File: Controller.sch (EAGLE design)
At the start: 45 parts, among them SW1 MULTICOLOR_BUTTON, SW2 MULTICOLOR_BUTTON, SW3 MULTICOLOR_BUTTON, SW4 MULTICOLOR_BUTTON, SW5 MULTICOLOR_BUTTON, SW6 MULTICOLOR_BUTTON, SW7 MULTICOLOR_BUTTON, SW8 MULTICOLOR_BUTTON, U1 ATMEGA328-PU, U2 DRV5053VAQLPGM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

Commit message: Added switch and LED
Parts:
- added R7: 1k, rcl:R-US_R1206
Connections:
- new net N$2: R7.2, U1.PCINT14/!RESET/PC6
- net +5V: now also R7.1
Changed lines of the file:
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@@
 <part name="C11" library="rcl" library_urn="urn:adsk.eagle:library:334" deviceset="C-US" device="C1206" package3d_urn="urn:adsk.eagle:package:23618/2" value="0.1u"/>
 <part name="GND4" library="supply1" library_urn="urn:adsk.eagle:library:371" deviceset="GND" device=""/>
+<part name="R7" library="rcl" library_urn="urn:adsk.eagle:library:334" deviceset="R-US_" device="R1206" package3d_urn="urn:adsk.eagle:package:23540/2" value="1k"/>
+<part name="P+11" library="supply1" library_urn="urn:adsk.eagle:library:371" deviceset="+5V" device=""/>
 </parts>
 <sheets>
@@
 <attribute name="VALUE" x="203.2" y="127" size="1.778" layer="96" rot="R90"/>
 </instance>
+<instance part="R7" gate="G$1" x="86.36" y="147.32" smashed="yes" rot="R270">
+<attribute name="NAME" x="80.2386" y="148.59" size="1.778" layer="95" rot="R270"/>
+<attribute name="VALUE" x="83.058" y="148.59" size="1.778" layer="96" rot="R270"/>
+</instance>
+<instance part="P+11" gate="1" x="86.36" y="157.48" smashed="yes">
+<attribute name="VALUE" x="83.82" y="152.4" size="1.778" layer="96" rot="R90"/>
+</instance>
 </instances>
 <busses>
@@
 <wire x1="175.26" y1="119.38" x2="175.26" y2="121.92" width="0.1524" layer="91"/>
 <junction x="175.26" y="121.92"/>
+</segment>
+<segment>
+<pinref part="P+11" gate="1" pin="+5V"/>
+<pinref part="R7" gate="G$1" pin="1"/>
+<wire x1="86.36" y1="154.94" x2="86.36" y2="152.4" width="0.1524" layer="91"/>
 </segment>
 </net>
@@
 </segment>
 </net>
+<net name="N$2" class="0">
+<segment>
+<pinref part="R7" gate="G$1" pin="2"/>
+<wire x1="86.36" y1="142.24" x2="86.36" y2="139.7" width="0.1524" layer="91"/>
+<pinref part="U1" gate="A" pin="PCINT14/!RESET/PC6"/>
+<wire x1="86.36" y1="139.7" x2="96.52" y2="139.7" width="0.1524" layer="91"/>
+</segment>
+</net>

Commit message: finished?
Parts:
- added J1: 282834-4, 282834-4:282834-4
- added J2: 282834-2, 282834-2:282834-2
- added J3: 825457-3, 825457-3:825457-3
- added R10: 150, rcl:R-US_R1206
- added R11: 475k, rcl:R-US_R1206
- added R12: 100k, rcl:R-US_R1206
- added R8, R9: 1k, rcl:R-US_R1206
- added SW9: 3PDT, Controller:3PDT
- added U$2: LED, Controller:LED
- added U$3: BSS138L, BSS138L:BSS138L
- added U6: (no value), Controller:SSM6P40TULFCT-ND
- C5: value 10U -> 10u
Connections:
- removed net N$2: R7.2, U1.PCINT14/!RESET/PC6
- removed net VBAT: C12.1, C13.1, U5.VIN
- new net CLK: J3.3, U1.PB5/SCK/PCINT5
- new net MISO: J3.1, R9.2, U1.PB4/MISO/PCINT4
- new net MOSI: J3.4, R8.2, U1.PB3/MOSI/OC2A/PCINT3
- new net N$10: J1.2, SW92.P, SW93.S
- new net N$11: J1.3, SW93.P
- new net N$12: SW93.O, U6G$2.D
- new net N$13: J2.1, R12.2, U6G$1.S, U6G$2.S
- new net N$15: SW91.O, U6G$1.D
- new net N$19: R11.2, R12.1, U6G$1.G, U6G$2.G
- new net N$5: U$4.GROUND1, U$6.GROUND1
- new net N$6: U$3.G, U1./PCINT20/XCK/T0/PD4
- new net N$7: U$2.P$2, U$3.D
- new net N$8: R10.2, U$2.P$1
- new net N$9: J1.1, SW91.P
- new net RESET: J3.5, R7.2, U1.PCINT14/!RESET/PC6
- new net VCC: C12.1, C13.1, SW91.S, U5.VIN
- net +5V: now also J3.2, R10.1, R8.1, R9.1, U5.4
- net GND: now also J1.4, J2.2, J3.6, R11.1, SW92.O, U$3.S, U$4.GROUND, U$6.GROUND
- net R4: now also U1.PCINT23/AIN1/PD7; no longer U1.PB3/MOSI/OC2A/PCINT3
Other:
- note added: "Power"
- moved on the sheet: C10, C12, C13, C7, C8, C9, U4, U5

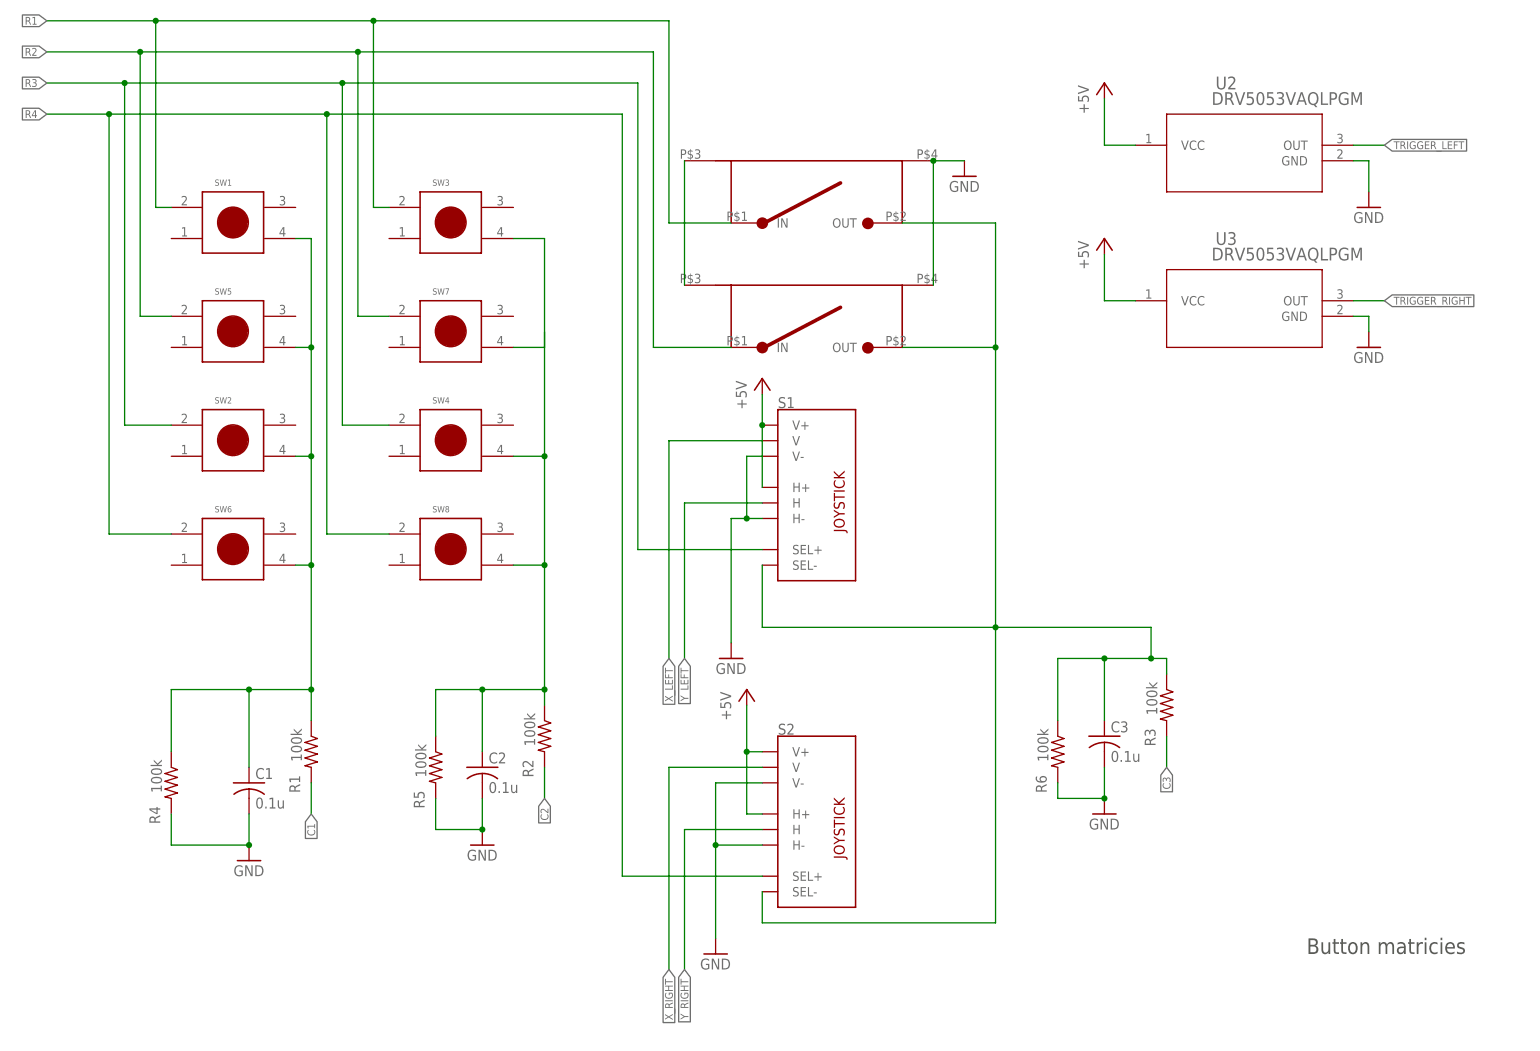
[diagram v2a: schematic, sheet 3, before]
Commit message: Added diodes and made traces 10 mills
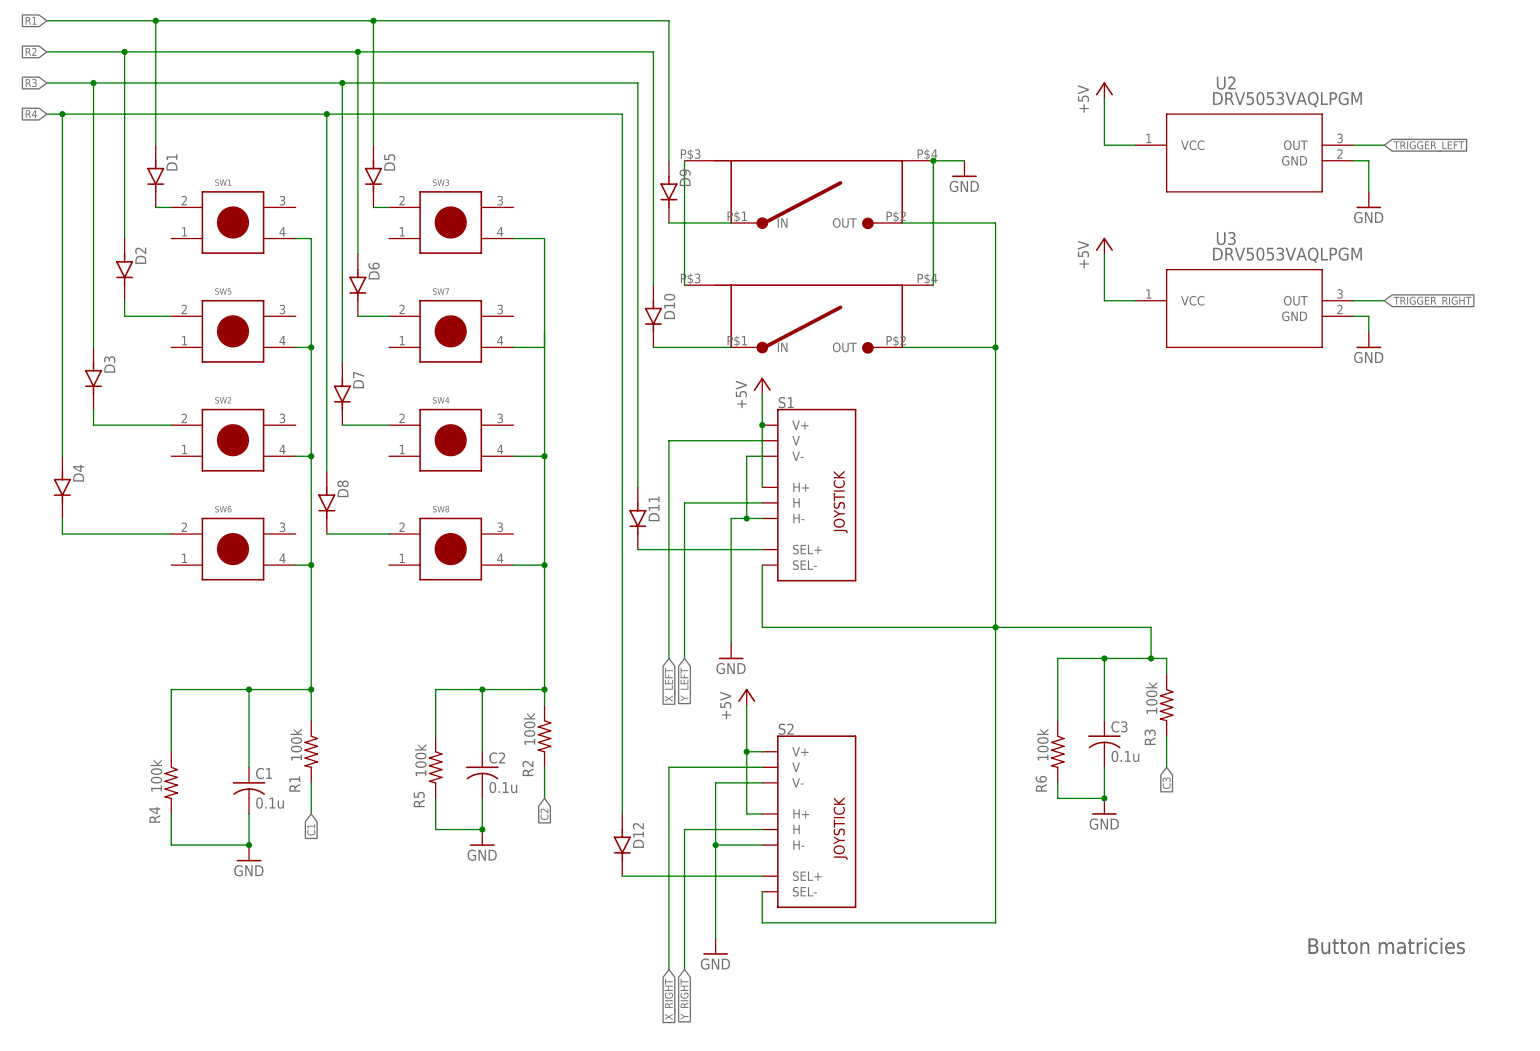
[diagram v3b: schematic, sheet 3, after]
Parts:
- added D1, D10, D11, D12, D2, D3, D4, D5, D6, D7, D8, D9: 1N4148, 1N4148:1N4148
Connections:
- new net N$16: D3.C, SW2.P$1
- new net N$18: D2.C, SW5.P$1
- new net N$2: D4.C, SW6.P$1
- new net N$20: D1.C, SW1.P$1
- new net N$21: D6.C, SW7.P$1
- new net N$22: D7.C, SW4.P$1
- new net N$23: D8.C, SW8.P$1
- new net N$24: D9.C, U$4.IN
- new net N$25: D5.C, SW3.P$1
- new net N$26: D10.C, U$6.IN
- new net N$27: D11.C, S1.SEL+
- new net N$28: D12.C, S2.SEL+
- net R1: now also D1.A, D5.A, D9.A; no longer SW1.P$1, SW3.P$1, U$4.IN
- net R2: now also D10.A, D2.A, D6.A; no longer SW5.P$1, SW7.P$1, U$6.IN
- net R3: now also D11.A, D3.A, D7.A; no longer S1.SEL+, SW2.P$1, SW4.P$1
- net R4: now also D12.A, D4.A, D8.A; no longer S2.SEL+, SW6.P$1, SW8.P$1
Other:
- note added: "Atmega328p"
- note removed: "Atmega2560"

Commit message: Read Desc.
* Moved Bumpers 3mm lower
* changed TO diodes to SMD
* Chnaged BOM to shorter actuator buttons
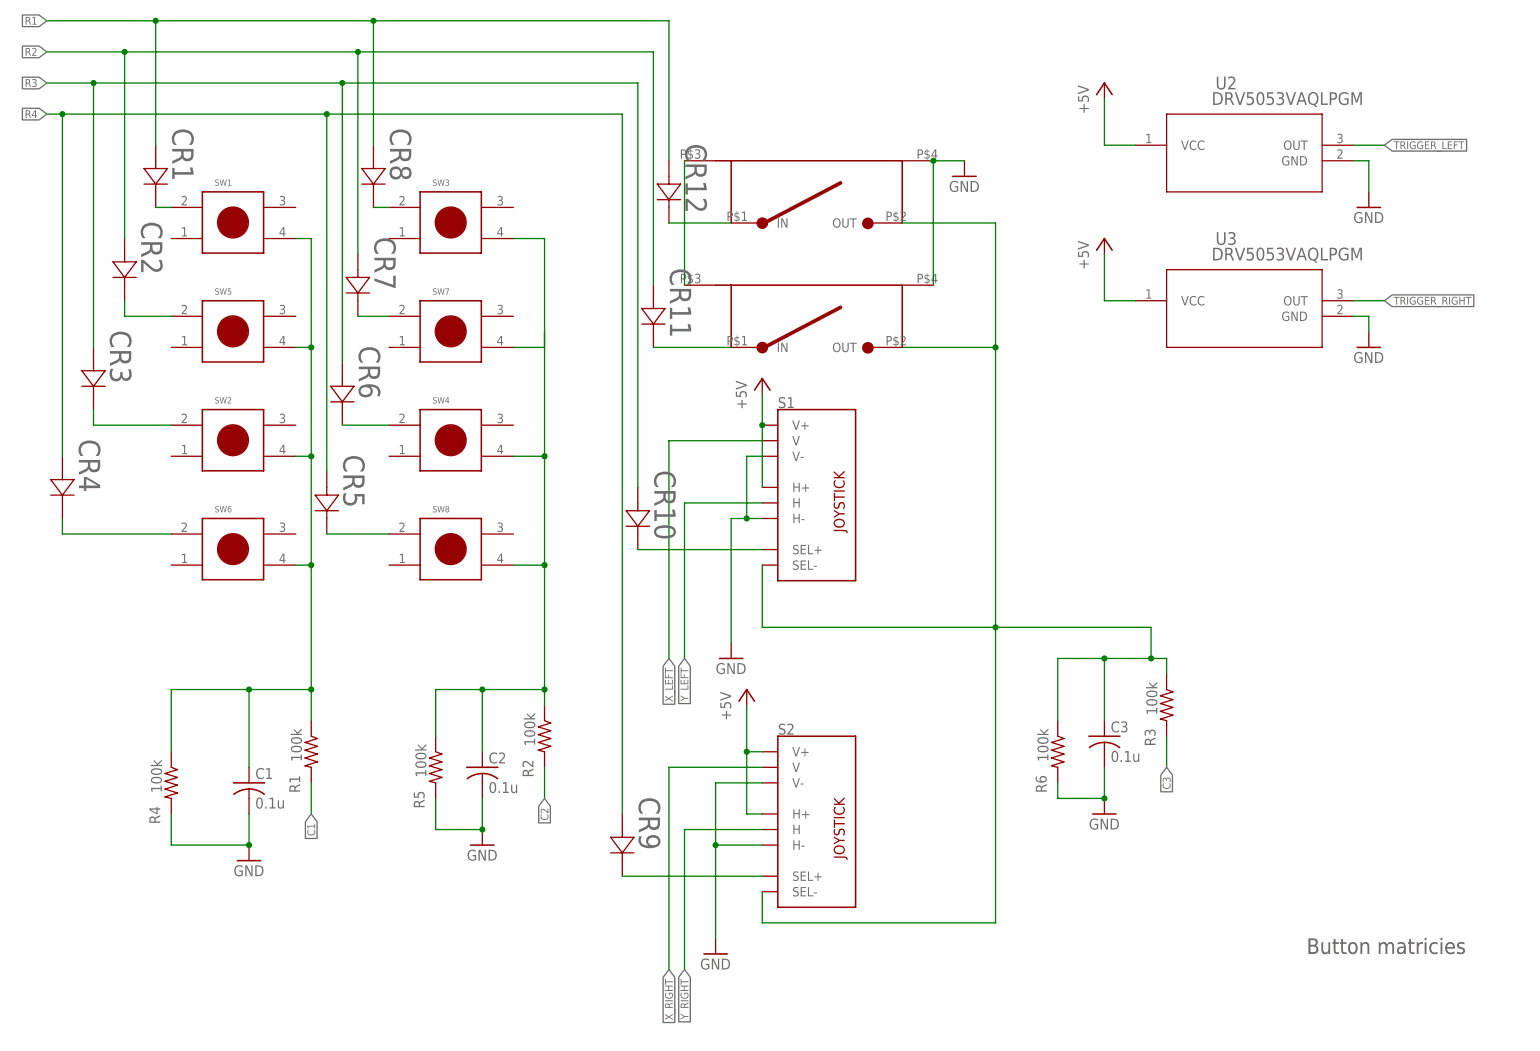
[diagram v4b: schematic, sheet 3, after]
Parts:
- removed D1, D10, D11, D12, D2, D3, D4, D5, D6, D7, D8, D9: 1N4148, 1N4148:1N4148
- added CR1, CR10, CR11, CR12, CR2, CR3, CR4, CR5, CR6, CR7, CR8, CR9: MSS1P6-M3/89ADIODE_MSP3V3-M, Controller:MSS1P6-M3/89ADIODE_MSP3V3-M
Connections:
- net N$16: now also CR3.1; no longer D3.C
- net N$18: now also CR2.1; no longer D2.C
- net N$2: now also CR4.1; no longer D4.C
- net N$20: now also CR1.1; no longer D1.C
- net N$21: now also CR7.1; no longer D6.C
- net N$22: now also CR6.1; no longer D7.C
- net N$23: now also CR5.1; no longer D8.C
- net N$24: now also CR12.1; no longer D9.C
- net N$25: now also CR8.1; no longer D5.C
- net N$26: now also CR11.1; no longer D10.C
- net N$27: now also CR10.1; no longer D11.C
- net N$28: now also CR9.1; no longer D12.C
- net R1: now also CR1.2, CR12.2, CR8.2; no longer D1.A, D5.A, D9.A
- net R2: now also CR11.2, CR2.2, CR7.2; no longer D10.A, D2.A, D6.A
- net R3: now also CR10.2, CR3.2, CR6.2; no longer D11.A, D3.A, D7.A
- net R4: now also CR4.2, CR5.2, CR9.2; no longer D12.A, D4.A, D8.A
